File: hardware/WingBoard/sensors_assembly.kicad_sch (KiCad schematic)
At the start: 11 parts

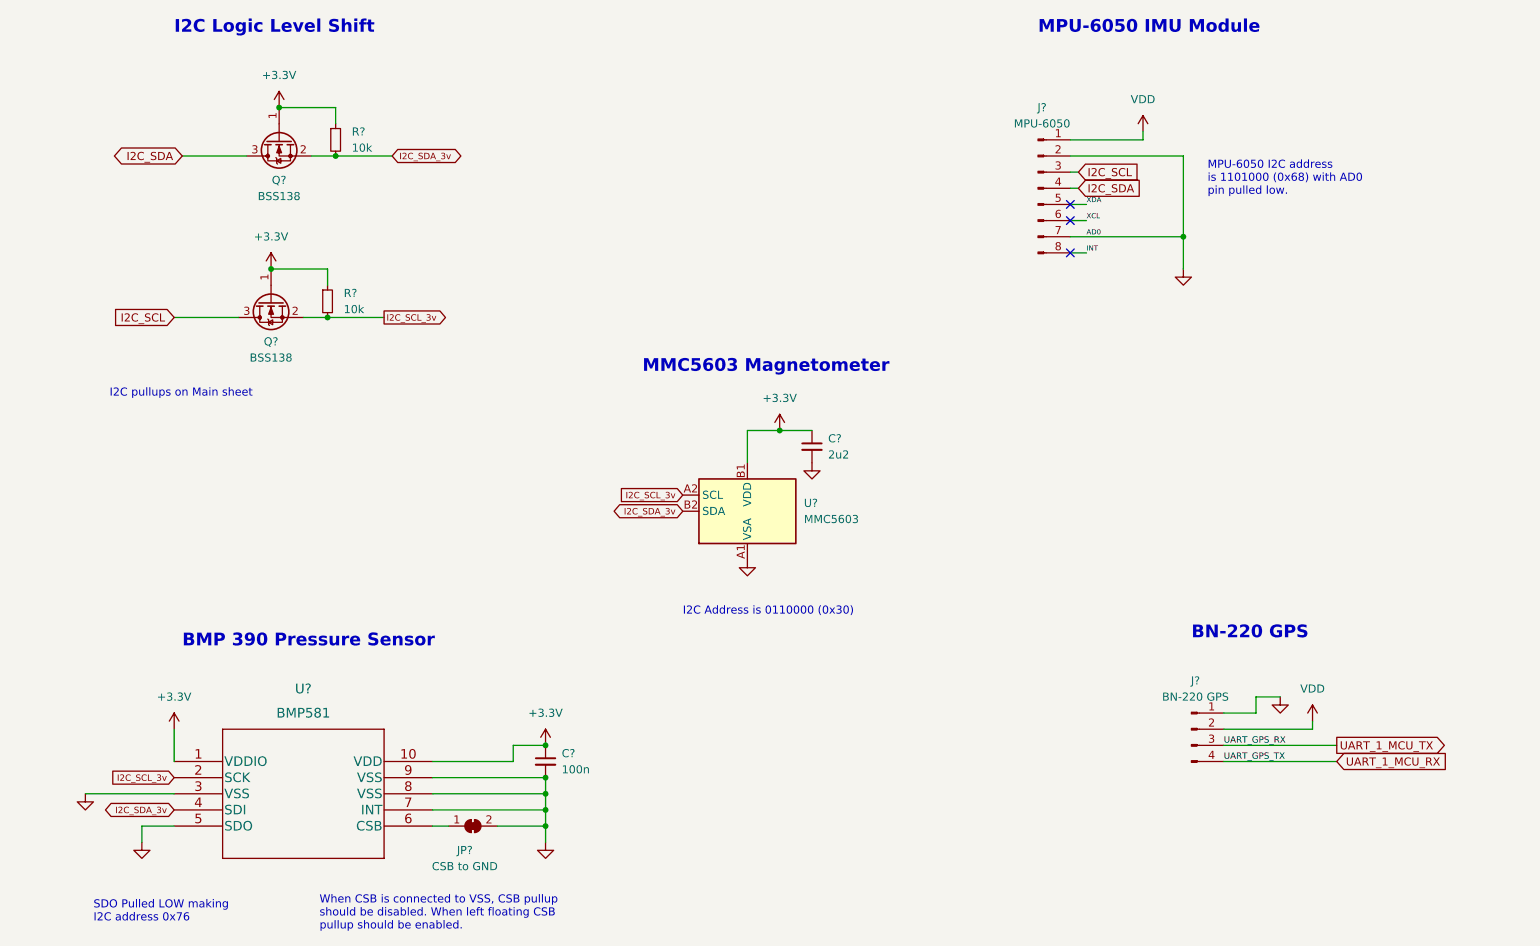
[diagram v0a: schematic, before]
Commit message: Added extra I2C headers to the schematic.
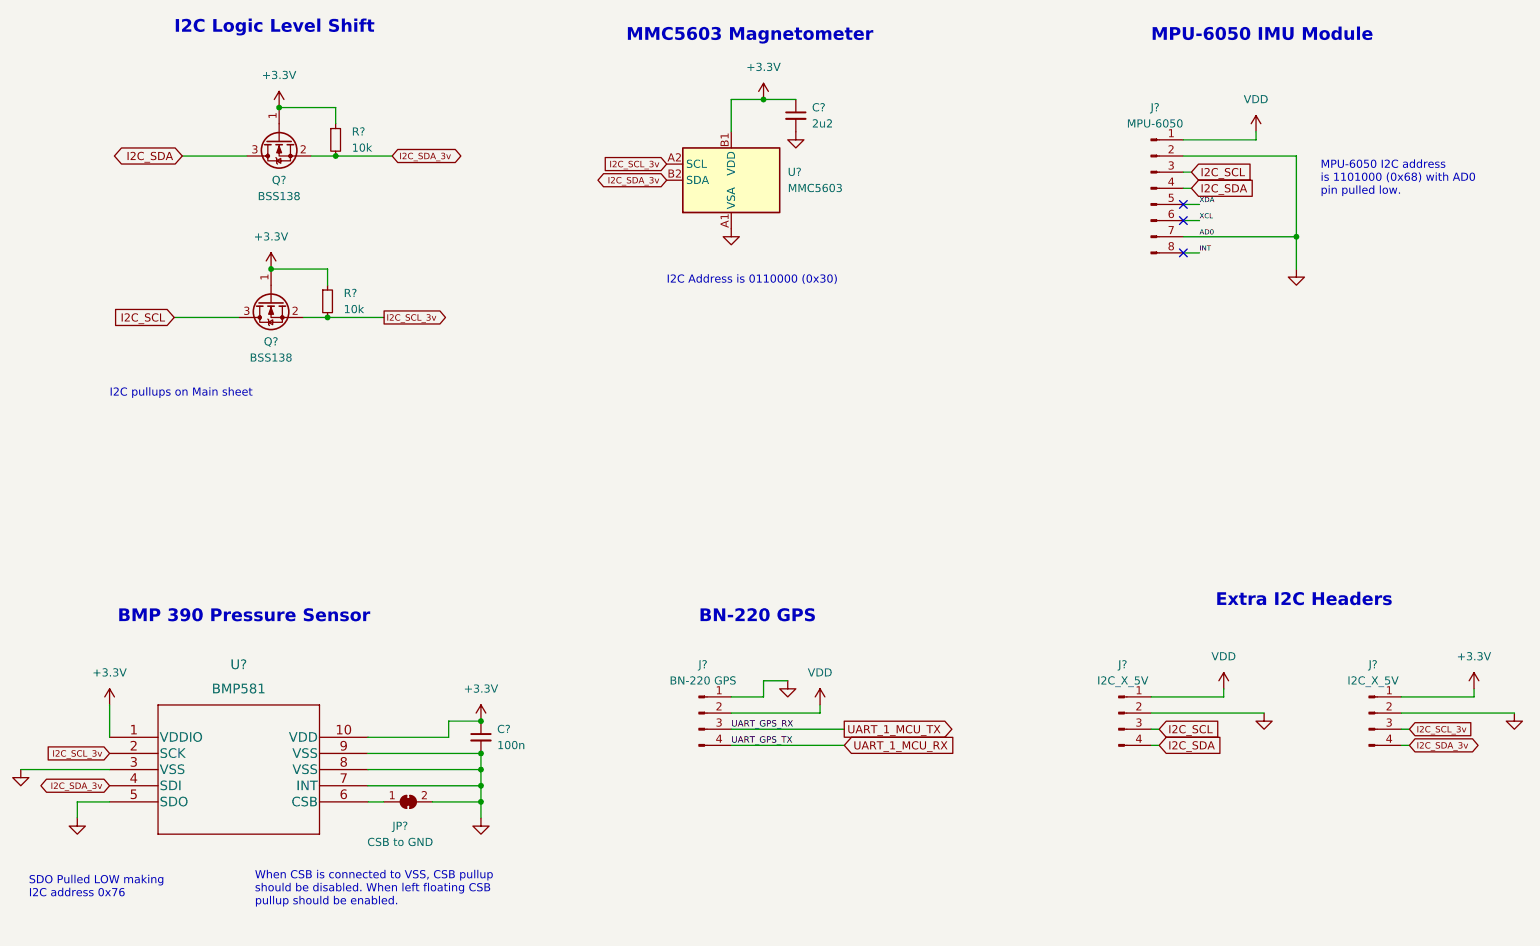
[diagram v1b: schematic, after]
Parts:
- added J? (x2): I2C_X_5V, symbol Connector:Conn_01x04_Male
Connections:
- net +3V3: now also J?.1 (Pin_1)
- net GND: now also J?.2 (Pin_2), J?.2 (Pin_2)
- net I2C_SCL: now also J?.3 (Pin_3)
- net I2C_SCL_3v: now also J?.3 (Pin_3)
- net I2C_SDA: now also J?.4 (Pin_4)
- net I2C_SDA_3v: now also J?.4 (Pin_4)
- net VDD: now also J?.1 (Pin_1)
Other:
- note added: "Extra I2C Headers"
- moved on the sheet: C?, J?, JP?, U?

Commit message: Hardware update: status LEDs, DIP switches, & test points.
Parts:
- added TP301: TP_SDA_3.3v, symbol Connector:TestPoint
- added TP302: TP_SCL_3.3v, symbol Connector:TestPoint
- J304: renamed from J?; value I2C_X_5V -> I2C_X_3.3V
- gave numbers to parts that had none: 12
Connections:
- net I2C_SCL_3v: now also TP302.1
- net I2C_SDA_3v: now also TP301.1

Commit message: Minor hardware design updates and assigned PCB footprints
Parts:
- C301, C302: footprint (none) -> Capacitor_SMD:C_0805_2012Metric_Pad1.18x1.45mm_HandSolder
- J301: footprint (none) -> Connector_PinHeader_2.54mm:PinHeader_1x08_P2.54mm_Vertical
- J302, J303, J304: footprint (none) -> Connector_JST:JST_SH_BM04B-SRSS-TB_1x04-1MP_P1.00mm_Vertical
- JP301: footprint (none) -> Jumper:SolderJumper-2_P1.3mm_Bridged_RoundedPad1.0x1.5mm
- Q301, Q302: footprint Package_TO_SOT_SMD:SOT-23 -> Resistor_SMD:R_0805_2012Metric_Pad1.20x1.40mm_HandSolder
- R301, R302: footprint (none) -> Resistor_SMD:R_0805_2012Metric_Pad1.20x1.40mm_HandSolder
- TP301, TP302: footprint (none) -> TestPoint:TestPoint_Pad_D1.5mm
- U302: footprint QFN10_BMP581_BOS -> Proj Sensors:BMP581
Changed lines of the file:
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@@
       (effects (font (size 1.27 1.27)) (justify left))
     )
-    (property "Footprint" "" (id 2) (at 96.52 46.99 0)
+    (property "Footprint" "TestPoint:TestPoint_Pad_D1.5mm" (id 2) (at 96.52 46.99 0)
       (effects (font (size 1.27 1.27)) hide)
     )
@@
     (property "Reference" "Q301" (id 0) (at 74.93 50.8 90))
     (property "Value" "BSS138" (id 1) (at 74.93 53.34 90))
-    (property "Footprint" "Package_TO_SOT_SMD:SOT-23" (id 2) (at 76.835 49.53 0)
+    (property "Footprint" "Resistor_SMD:R_0805_2012Metric_Pad1.20x1.40mm_HandSolder" (id 2) (at 76.835 49.53 0)
       (effects (font (size 1.27 1.27) italic) (justify left) hide)
     )
@@
     (property "Reference" "J304" (id 0) (at 247.015 127 0))
     (property "Value" "I2C_X_3.3V" (id 1) (at 247.015 129.54 0))
-    (property "Footprint" "" (id 2) (at 246.38 134.62 0)
+    (property "Footprint" "Connector_JST:JST_SH_BM04B-SRSS-TB_1x04-1MP_P1.00mm_Vertical" (id 2) (at 246.38 134.62 0)
       (effects (font (size 1.27 1.27)) hide)
     )
@@
       (effects (font (size 1.27 1.27)) (justify left))
     )
-    (property "Footprint" "" (id 2) (at 83.82 44.45 0)
+    (property "Footprint" "Resistor_SMD:R_0805_2012Metric_Pad1.20x1.40mm_HandSolder" (id 2) (at 83.82 44.45 0)
       (effects (font (size 1.27 1.27)) hide)
     )
@@
     (property "Reference" "JP301" (id 0) (at 93.98 152.4 0))
     (property "Value" "CSB to GND" (id 1) (at 93.98 154.94 0))
-    (property "Footprint" "" (id 2) (at 95.25 148.59 0)
+    (property "Footprint" "Jumper:SolderJumper-2_P1.3mm_Bridged_RoundedPad1.0x1.5mm" (id 2) (at 95.25 148.59 0)
       (effects (font (size 1.27 1.27)) hide)
     )
@@
       (effects (font (size 1.27 1.27)) (justify left))
     )
-    (property "Footprint" "" (id 2) (at 82.55 69.85 0)
+    (property "Footprint" "Resistor_SMD:R_0805_2012Metric_Pad1.20x1.40mm_HandSolder" (id 2) (at 82.55 69.85 0)
       (effects (font (size 1.27 1.27)) hide)
     )
@@
     (property "Reference" "Q302" (id 0) (at 73.66 76.2 90))
     (property "Value" "BSS138" (id 1) (at 73.66 78.74 90))
-    (property "Footprint" "Package_TO_SOT_SMD:SOT-23" (id 2) (at 75.565 74.93 0)
+    (property "Footprint" "Resistor_SMD:R_0805_2012Metric_Pad1.20x1.40mm_HandSolder" (id 2) (at 75.565 74.93 0)
       (effects (font (size 1.27 1.27) italic) (justify left) hide)
     )
@@
       (effects (font (size 1.27 1.27)) (justify left))
     )
-    (property "Footprint" "" (id 2) (at 95.25 72.39 0)
+    (property "Footprint" "TestPoint:TestPoint_Pad_D1.5mm" (id 2) (at 95.25 72.39 0)
       (effects (font (size 1.27 1.27)) hide)
     )
@@
       (effects (font (size 1.27 1.27)) (justify left))
     )
-    (property "Footprint" "" (id 2) (at 106.68 138.43 0)
+    (property "Footprint" "Capacitor_SMD:C_0805_2012Metric_Pad1.18x1.45mm_HandSolder" (id 2) (at 106.68 138.43 0)
       (effects (font (size 1.27 1.27)) hide)
     )
@@
       (effects (font (size 1.524 1.524)))
     )
-    (property "Footprint" "QFN10_BMP581_BOS" (id 2) (at 68.58 132.334 0)
+    (property "Footprint" "Proj Sensors:BMP581" (id 2) (at 68.58 132.334 0)
       (effects (font (size 1.524 1.524)) hide)
     )
@@
       (effects (font (size 1.27 1.27)) (justify left))
     )
-    (property "Footprint" "" (id 2) (at 156.21 40.64 0)
+    (property "Footprint" "Capacitor_SMD:C_0805_2012Metric_Pad1.18x1.45mm_HandSolder" (id 2) (at 156.21 40.64 0)
       (effects (font (size 1.27 1.27)) hide)
     )
@@
     (property "Reference" "J302" (id 0) (at 141.605 127 0))
     (property "Value" "BN-220 GPS" (id 1) (at 141.605 129.54 0))
-    (property "Footprint" "" (id 2) (at 140.97 134.62 0)
+    (property "Footprint" "Connector_JST:JST_SH_BM04B-SRSS-TB_1x04-1MP_P1.00mm_Vertical" (id 2) (at 140.97 134.62 0)
       (effects (font (size 1.27 1.27)) hide)
     )
@@
     (property "Reference" "J301" (id 0) (at 212.725 39.37 0))
     (property "Value" "MPU-6050" (id 1) (at 212.725 41.91 0))
-    (property "Footprint" "" (id 2) (at 212.09 52.07 0)
+    (property "Footprint" "Connector_PinHeader_2.54mm:PinHeader_1x08_P2.54mm_Vertical" (id 2) (at 212.09 52.07 0)
       (effects (font (size 1.27 1.27)) hide)
     )
@@
     (property "Reference" "J303" (id 0) (at 207.645 127 0))
     (property "Value" "I2C_X_5V" (id 1) (at 207.645 129.54 0))
-    (property "Footprint" "" (id 2) (at 207.01 134.62 0)
-      (effects (font (size 1.27 1.27)) hide)
-    )
+    (property "Footprint" "Connector_JST:JST_SH_BM04B-SRSS-TB_1x04-1MP_P1.00mm_Vertical" (id 2) (at 207.01 134.62 0)
+      (effects (font (size 1.27 1.27)) hide)
+    )

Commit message: PCB rough layout done.
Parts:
- Q301, Q302: footprint Resistor_SMD:R_0805_2012Metric_Pad1.20x1.40mm_HandSolder -> Package_TO_SOT_SMD:SOT-23
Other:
- note added: "I2C pullups are on the main sheet Logic level shifting based on the NXP paper "Level shifting techniques in I2C-bus design""
- note removed: "I2C pullups on Main sheet"
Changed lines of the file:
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@@
     (stroke (width 0) (type default) (color 0 0 0 0))
   )
-  (text "I2C pullups on Main sheet" (at 48.26 85.09 0)
+  (text "I2C pullups are on the main sheet\nLogic level shifting based on the\nNXP paper \"Level shifting techniques in I2C-bus design\""
+    (at 50.8 88.9 0)
     (effects (font (size 1.27 1.27)) (justify left bottom))
   )
@@
     (property "Reference" "Q301" (id 0) (at 74.93 50.8 90))
     (property "Value" "BSS138" (id 1) (at 74.93 53.34 90))
-    (property "Footprint" "Resistor_SMD:R_0805_2012Metric_Pad1.20x1.40mm_HandSolder" (id 2) (at 76.835 49.53 0)
+    (property "Footprint" "Package_TO_SOT_SMD:SOT-23" (id 2) (at 76.835 49.53 0)
       (effects (font (size 1.27 1.27) italic) (justify left) hide)
     )
@@
     (property "Reference" "Q302" (id 0) (at 73.66 76.2 90))
     (property "Value" "BSS138" (id 1) (at 73.66 78.74 90))
-    (property "Footprint" "Resistor_SMD:R_0805_2012Metric_Pad1.20x1.40mm_HandSolder" (id 2) (at 75.565 74.93 0)
+    (property "Footprint" "Package_TO_SOT_SMD:SOT-23" (id 2) (at 75.565 74.93 0)
       (effects (font (size 1.27 1.27) italic) (justify left) hide)
     )

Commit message: Hardware layout v0.1 complete.
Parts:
- removed TP301: TP_SDA_3.3v, TestPoint:TestPoint_Pad_D1.5mm, symbol Connector:TestPoint
- removed TP302: TP_SCL_3.3v, TestPoint:TestPoint_Pad_D1.5mm, symbol Connector:TestPoint
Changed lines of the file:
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@@
 (kicad_sch (version 20211123) (generator eeschema)
   (paper "A4")
-  (junction (at 90.17 72.39) (diameter 0) (color 0 0 0 0)
-  )
   (junction (at 106.68 146.05) (diameter 0) (color 0 0 0 0)
   )
@@
   )
   (junction (at 106.68 148.59) (diameter 0) (color 0 0 0 0)
-  )
-  (junction (at 91.44 46.99) (diameter 0) (color 0 0 0 0)
   )
   (junction (at 82.55 72.39) (diameter 0) (color 0 0 0 0)
@@
     (stroke (width 0) (type default) (color 0 0 0 0))
   )
-  (wire (pts (xy 91.44 46.99) (xy 92.71 46.99))
-    (stroke (width 0) (type default) (color 0 0 0 0))
-  )
-  (wire (pts (xy 90.17 72.39) (xy 91.44 72.39))
-    (stroke (width 0) (type default) (color 0 0 0 0))
-  )
   (wire (pts (xy 80.01 46.99) (xy 83.82 46.99))
     (stroke (width 0) (type default) (color 0 0 0 0))
@@
     (stroke (width 0) (type default) (color 0 0 0 0))
   )
-  (wire (pts (xy 82.55 72.39) (xy 90.17 72.39))
+  (wire (pts (xy 82.55 72.39) (xy 91.44 72.39))
     (stroke (width 0) (type default) (color 0 0 0 0))
   )
@@
     (stroke (width 0) (type default) (color 0 0 0 0))
   )
-  (wire (pts (xy 83.82 46.99) (xy 91.44 46.99))
+  (wire (pts (xy 83.82 46.99) (xy 92.71 46.99))
     (stroke (width 0) (type default) (color 0 0 0 0))
   )
@@
     )
     (property "Datasheet" "" (id 3) (at 160.02 133.35 0)
-      (effects (font (size 1.27 1.27)) hide)
-    )
-    (pin "1")
-  )
-  (symbol (lib_id "Connector:TestPoint") (at 91.44 46.99 0) (unit 1)
-    (in_bom yes) (on_board yes)
-    (property "Reference" "TP301" (id 0) (at 88.9 38.1 0)
-      (effects (font (size 1.27 1.27)) (justify left))
-    )
-    (property "Value" "TP_SDA_3.3v" (id 1) (at 88.9 40.64 0)
-      (effects (font (size 1.27 1.27)) (justify left))
-    )
-    (property "Footprint" "TestPoint:TestPoint_Pad_D1.5mm" (id 2) (at 96.52 46.99 0)
-      (effects (font (size 1.27 1.27)) hide)
-    )
-    (property "Datasheet" "~" (id 3) (at 96.52 46.99 0)
       (effects (font (size 1.27 1.27)) hide)
     )
@@
     (pin "3")
   )
-  (symbol (lib_id "Connector:TestPoint") (at 90.17 72.39 0) (unit 1)
-    (in_bom yes) (on_board yes)
-    (property "Reference" "TP302" (id 0) (at 91.44 66.04 0)
-      (effects (font (size 1.27 1.27)) (justify left))
-    )
-    (property "Value" "TP_SCL_3.3v" (id 1) (at 91.44 68.58 0)
-      (effects (font (size 1.27 1.27)) (justify left))
-    )
-    (property "Footprint" "TestPoint:TestPoint_Pad_D1.5mm" (id 2) (at 95.25 72.39 0)
-      (effects (font (size 1.27 1.27)) hide)
-    )
-    (property "Datasheet" "~" (id 3) (at 95.25 72.39 0)
-      (effects (font (size 1.27 1.27)) hide)
-    )
-    (pin "1")
-  )
   (symbol (lib_id "Device:C_Small") (at 106.68 138.43 0) (unit 1)
